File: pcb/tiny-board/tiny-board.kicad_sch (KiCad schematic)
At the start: 22 parts, among them J1 USB_B, J2 EXPBUS1, J4 Atmel-JTAG-10, SW1 RESET, SW2 NMI, SW3 SW_SPDT, U1 74AC14, U2 W65C02, U3 ATF1502AS-PLCC44, X1 14 MHz

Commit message: Saving tiny board design
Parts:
- removed J4: Atmel-JTAG-10, Connector_IDC:IDC-Header_2x05_P2.54mm_Vertical, symbol atf1504_plcc44_breakout:Atmel-JTAG-10
- removed U3: ATF1502AS-PLCC44, Package_LCC:PLCC-44_THT-Socket, symbol atf1504as-plcc44:ATF1504AS-xJx44
- added C2: 100nF, Capacitor_THT:C_Disc_D5.0mm_W2.5mm_P5.00mm, symbol Device:C
- added U3: CD74HC688, Package_DIP:DIP-20_W7.62mm_Socket, symbol 74xx:74HC688
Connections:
- net A10: now also U3.6 (P2)
- net A11: now also U3.8 (P3)
- net A12: now also U3.11 (P4)
- net A13: now also U3.13 (P5)
- net A14: now also U3.15 (P6)
- net A15: now also U3.17 (P7)
- net A8: now also U3.2 (P0)
- net A9: now also U3.4 (P1)
- net GND: now also C2.2, U3.1 (G), U3.10 (GND), U3.18 (R7)
- net VCC: now also C2.1, U3.12 (R4), U3.14 (R5), U3.16 (R6), U3.20 (VCC), U3.3 (R0), U3.5 (R1), U3.7 (R2), U3.9 (R3)
- net ~{I/O}: now also U3.19 (P=R)
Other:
- note added: "0x7F"
- note added: "0x7FXX"
- note added: "Single 74HC688 is used to map 0x7F00 - 0x7FF as the I/O space."

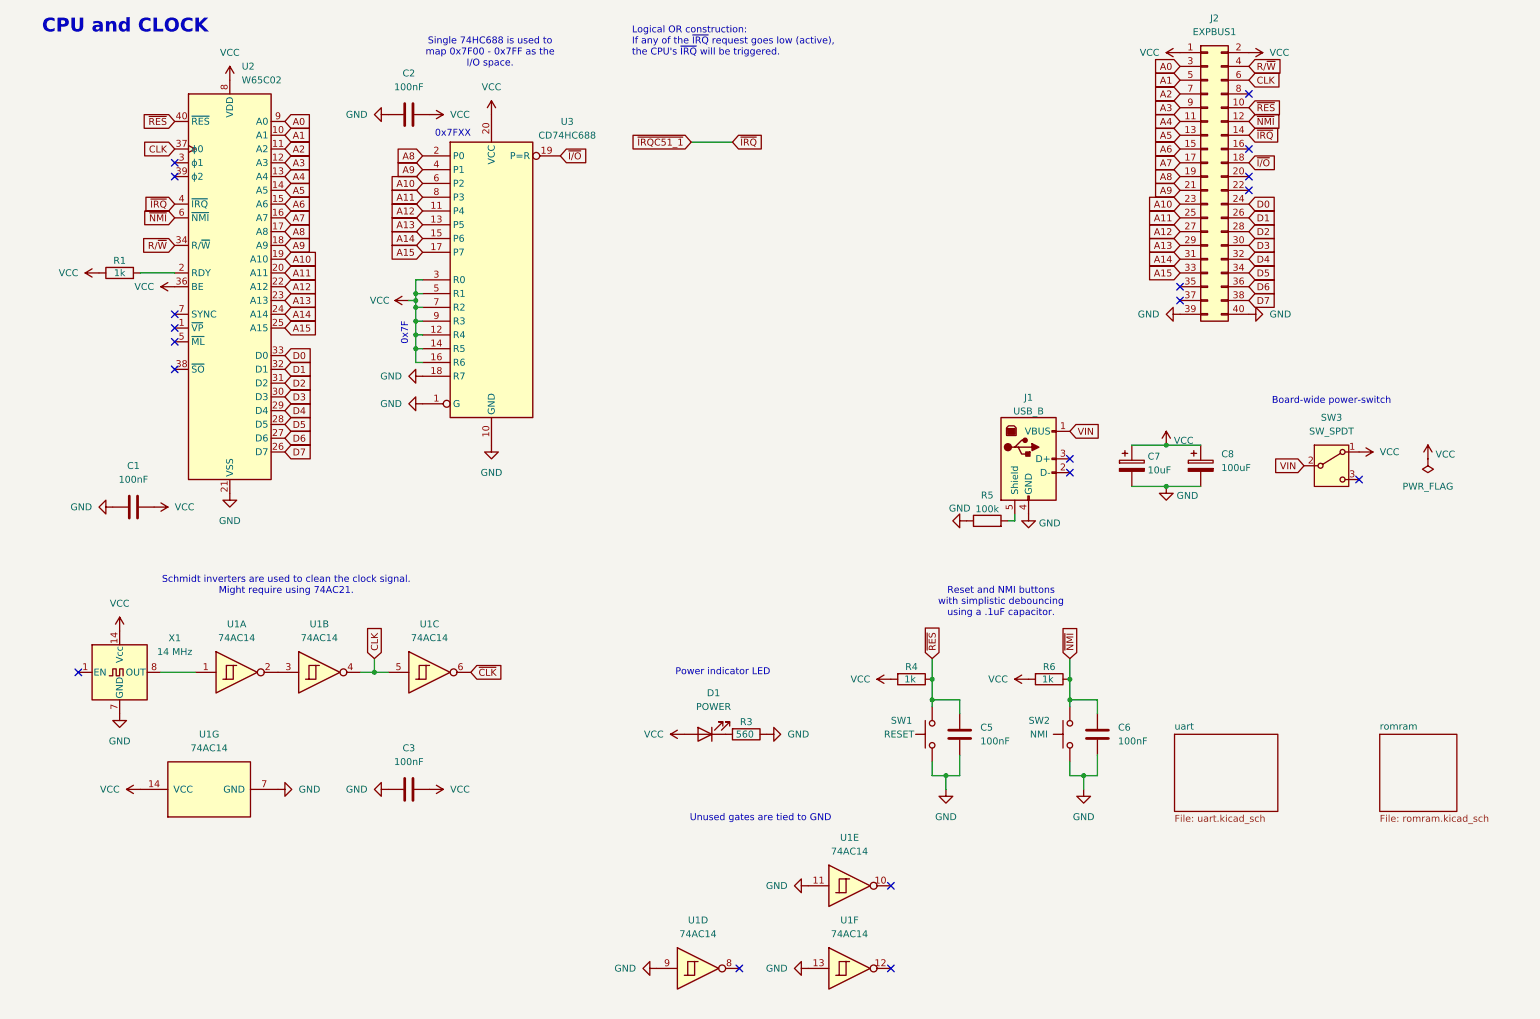
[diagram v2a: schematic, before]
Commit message: Revising TINY board and writing CUPL
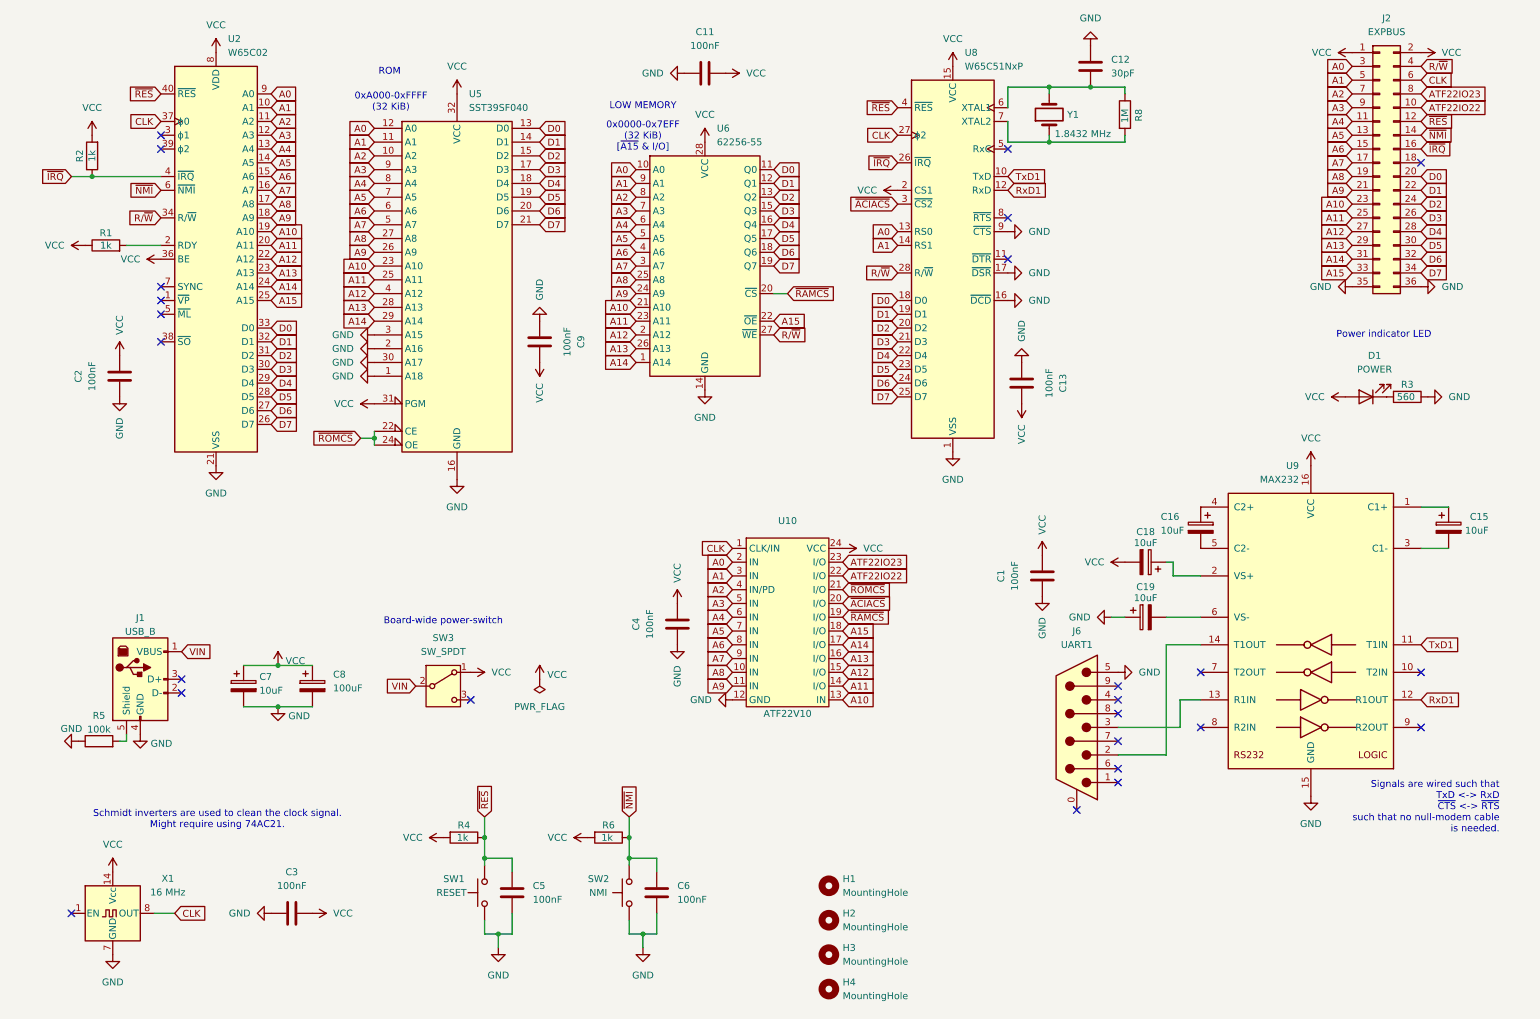
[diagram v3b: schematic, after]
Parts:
- removed J2: EXPBUS1, Connector_PinHeader_2.54mm:PinHeader_2x20_P2.54mm_Vertical, symbol Connector_Generic:Conn_02x20_Odd_Even
- removed U1: 74AC14, Package_DIP:DIP-14_W7.62mm_Socket, symbol 74xx:74HC14
- removed U3: CD74HC688, Package_DIP:DIP-20_W7.62mm_Socket, symbol 74xx:74HC688
- added C11, C13, C4, C9: 100nF, Capacitor_THT:C_Disc_D5.0mm_W2.5mm_P5.00mm, symbol Device:C
- added C12: 30pF, Capacitor_THT:C_Disc_D5.0mm_W2.5mm_P5.00mm, symbol Device:C
- added C15, C16, C18, C19: 10uF, Capacitor_THT:CP_Radial_D5.0mm_P2.50mm, symbol Device:C_Polarized
- added H1, H2, H3, H4: MountingHole, MountingHole:MountingHole_3.2mm_M3_DIN965_Pad_TopOnly, symbol Mechanical:MountingHole
- added J2: EXPBUS, Connector_PinHeader_2.54mm:PinHeader_2x18_P2.54mm_Vertical, symbol Connector_Generic:Conn_02x18_Odd_Even
- added J6: UART1, Connector_Dsub:DSUB-9_Pins_Horizontal_P2.77x2.84mm_EdgePinOffset4.94mm_Housed_MountingHolesOffset4.94mm, symbol Connector:DE9_Pins_MountingHoles
- added R2: 1k, Resistor_THT:R_Axial_DIN0207_L6.3mm_D2.5mm_P7.62mm_Horizontal, symbol Device:R
- added R8: 1M, Resistor_THT:R_Axial_DIN0207_L6.3mm_D2.5mm_P7.62mm_Horizontal, symbol Device:R
- added U10: ATF22V10, Package_DIP:DIP-24_W7.62mm_Socket, symbol atf22v10:ATF22V10
- added U5: SST39SF040, Package_DIP:DIP-32_W15.24mm_Socket, symbol Memory_Flash:SST39SF040
- added U6: 62256-55, Package_DIP:DIP-28_W15.24mm_Socket, symbol Memory_RAM:CY62256-70PC
- added U8: W65C51NxP, Package_DIP:DIP-28_W15.24mm_Socket, symbol 65xx-library:W65C51NxP
- added U9: MAX232, Package_DIP:DIP-16_W7.62mm_Socket, symbol Interface_UART:MAX232
- added Y1: 1.8432 MHz, Crystal:Crystal_HC50_Vertical, symbol Device:Crystal
- C7: footprint Capacitor_THT:CP_Radial_D6.3mm_P2.50mm -> Capacitor_THT:CP_Radial_D5.0mm_P2.50mm
- X1: value 14 MHz -> 16 MHz
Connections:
- net A0: now also J2.3 (Pin_3), U10.2 (IN), U5.12 (A0), U6.10 (A0), U8.13 (RS0)
- net A1: now also J2.5 (Pin_5), U10.3 (IN), U5.11 (A1), U6.9 (A1), U8.14 (RS1)
- net A10: now also J2.23 (Pin_23), U10.13 (IN), U5.23 (A10), U6.21 (A10)
- net A11: now also J2.25 (Pin_25), U10.14 (I/O), U5.25 (A11), U6.23 (A11)
- net A12: now also J2.27 (Pin_27), U10.15 (I/O), U5.4 (A12), U6.2 (A12)
- net A13: now also J2.29 (Pin_29), U10.16 (I/O), U5.28 (A13), U6.26 (A13)
- net A14: now also J2.31 (Pin_31), U10.17 (I/O), U5.29 (A14), U6.1 (A14)
- net A15: now also J2.33 (Pin_33), U10.18 (I/O), U6.22 (~{OE})
- net A2: now also J2.7 (Pin_7), U10.4 (IN/PD), U5.10 (A2), U6.8 (A2)
- net A3: now also J2.9 (Pin_9), U10.5 (IN), U5.9 (A3), U6.7 (A3)
- net A4: now also J2.11 (Pin_11), U10.6 (IN), U5.8 (A4), U6.6 (A4)
- net A5: now also J2.13 (Pin_13), U10.7 (IN), U5.7 (A5), U6.5 (A5)
- net A6: now also J2.15 (Pin_15), U10.8 (IN), U5.6 (A6), U6.4 (A6)
- net A7: now also J2.17 (Pin_17), U10.9 (IN), U5.5 (A7), U6.3 (A7)
- net A8: now also J2.19 (Pin_19), U10.10 (IN), U5.27 (A8), U6.25 (A8)
- net A9: now also J2.21 (Pin_21), U10.11 (IN), U5.26 (A9), U6.24 (A9)
- net CLK: now also X1.8 (OUT), J2.6 (Pin_6), U10.1 (CLK/IN), U8.27 (ϕ2)
- net D0: now also J2.20 (Pin_20), U5.13 (D0), U6.11 (Q0), U8.18 (D0)
- net D1: now also J2.22 (Pin_22), U5.14 (D1), U6.12 (Q1), U8.19 (D1)
- net D2: now also J2.24 (Pin_24), U5.15 (D2), U6.13 (Q2), U8.20 (D2)
- net D3: now also J2.26 (Pin_26), U5.17 (D3), U6.15 (Q3), U8.21 (D3)
- net D4: now also J2.28 (Pin_28), U5.18 (D4), U6.16 (Q4), U8.22 (D4)
- net D5: now also J2.30 (Pin_30), U5.19 (D5), U6.17 (Q5), U8.23 (D5)
- net D6: now also J2.32 (Pin_32), U5.20 (D6), U6.18 (Q6), U8.24 (D6)
- net D7: now also J2.34 (Pin_34), U5.21 (D7), U6.19 (Q7), U8.25 (D7)
- net GND: now also C11.2, C12.1, C13.2, C19.1, C4.2, C9.2, J2.35 (Pin_35), J2.36 (Pin_36), J6.5, U10.12 (GND), U5.1 (A18), U5.16 (GND), U5.2 (A16), U5.3 (A15), U5.30 (A17), U6.14 (GND), U8.1 (VSS), U8.16 (~{DCD}), U8.17 (~{DSR}), U8.9 (~{CTS}), U9.15 (GND)
- net R/~{W}: now also J2.4 (Pin_4), U6.27 (~{WE}), U8.28 (R/~{W})
- net VCC: now also C11.1, C13.1, C18.2, C4.1, C9.1, J2.1 (Pin_1), J2.2 (Pin_2), R2.2, U10.24 (VCC), U5.31 (PGM), U5.32 (VCC), U6.28 (VCC), U8.15 (VCC), U8.2 (CS1), U9.16 (VCC)
- net ~{NMI}: now also J2.14 (Pin_14)
- net ~{RES}: now also J2.12 (Pin_12), U8.4 (~{RES})
- net ~{IRQC51_1} renamed ~{IRQ}
- net ~{IRQ}: now also J2.16 (Pin_16), R2.1, U8.26 (~{IRQ})
- new net: R8.2, U8.7 (XTAL2), Y1.1
- new net: C12.2, R8.1, U8.6 (XTAL1), Y1.2
- new net: C15.1, U9.1 (C1+)
- new net: J6.3, U9.13 (R1IN)
- new net: J6.2, U9.14 (T1OUT)
- new net: C18.1, U9.2 (VS+)
- new net: C15.2, U9.3 (C1-)
- new net: C16.1, U9.4 (C2+)
- new net: C16.2, U9.5 (C2-)
- new net: C19.2, U9.6 (VS-)
- new net ATF22IO22: J2.10 (Pin_10), U10.22 (I/O)
- new net ATF22IO23: J2.8 (Pin_8), U10.23 (I/O)
- new net RxD1: U8.12 (RxD), U9.12 (R1OUT)
- new net TxD1: U8.10 (TxD), U9.11 (T1IN)
- new net ~{ACIACS}: U10.20 (I/O), U8.3 (~{CS2})
- new net ~{RAMCS}: U10.19 (I/O), U6.20 (~{CS})
- new net ~{ROMCS}: U10.21 (I/O), U5.22 (CE), U5.24 (OE)
- no-connect marks 19 -> 25
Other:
- removed sheet romram
- removed sheet uart
- note added: "0x0000-0x7EFF (32 KiB) [~{A15} & I/O]"
- note added: "0xA000-0xFFFF (32 KiB)"
- note added: "LOW MEMORY"
- note added: "ROM"
- note added: "Signals are wired such that TxD <-> RxD ~{CTS} <-> ~{RTS} such that no null-modem cable is needed."
- note removed: "0x7F"
- note removed: "0x7FXX"
- note removed: "CPU and CLOCK"
- note removed: "Logical OR construction: If any of the ~{IRQ} request goes low (active), the CPU's ~{IRQ} will be triggered."
- note removed: "Reset and NMI buttons with simplistic debouncing using a .1uF capacitor."
- note removed: "Single 74HC688 is used to map 0x7F00 - 0x7FF as the I/O space."
- note removed: "Unused gates are tied to GND"
- title: ByteCradle 6502 - CPU & CLOCK -> ByteCradle 6502 - TINY
- moved on the sheet: C1, C3, C5, C6, C7, C8, D1, J1, R1, R3, R4, R5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

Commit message: Integrating monitor
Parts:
- U5: symbol Memory_Flash:SST39SF040 -> Memory_Flash:SST39SF010
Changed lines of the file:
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@@
 	)
 	(symbol
-		(lib_id "Memory_Flash:SST39SF040")
+		(lib_id "Memory_Flash:SST39SF010")
 		(at 90.17 66.04 0)
 		(unit 1)
@@
 		(fields_autoplaced yes)
 		(property "Reference" "U5"
-			(at 92.3641 29.21 0)
+			(at 92.3133 29.21 0)
 			(effects
 				(font
@@
 		)
 		(property "Value" "SST39SF040"
-			(at 92.3641 31.75 0)
+			(at 92.3133 31.75 0)
 			(effects
 				(font
@@
 			)
 		)
-		(property "Description" "Silicon Storage Technology (SSF) 512k x 8 Flash ROM"
+		(property "Description" "Silicon Storage Technology (SSF) 128k x 8 Flash ROM"
 			(at 90.17 66.04 0)
 			(effects

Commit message: Integrating CIA CPLD for tiny board
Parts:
- U5: value SST39SF040 -> SST39SF010
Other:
- note added: "0x8000-0xFFFF (32 KiB)"
- note removed: "0xA000-0xFFFF (32 KiB)"
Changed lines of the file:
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@@
 		)
 	)
-	(text "0xA000-0xFFFF\n(32 KiB)"
+	(text "0x8000-0xFFFF\n(32 KiB)"
 		(exclude_from_sim no)
 		(at 77.978 30.734 0)
@@
 			)
 		)
-		(property "Value" "SST39SF040"
+		(property "Value" "SST39SF010"
 			(at 92.3133 31.75 0)
 			(effects

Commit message: Revising board and integrating DS1813
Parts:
- removed C5: 100nF, Capacitor_THT:C_Disc_D5.0mm_W2.5mm_P5.00mm, symbol Device:C
- removed R4: 1k, Resistor_THT:R_Axial_DIN0207_L6.3mm_D2.5mm_P7.62mm_Horizontal, symbol Device:R
- added U11: DS1813, Package_TO_SOT_THT:TO-92, symbol Connector:Conn_01x03_Pin
- C8: value 100uF -> 220uF
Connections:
- net GND: now also U11.3 (Pin_3)
- net VCC: now also U11.2 (Pin_2)
- net ~{RES}: now also U11.1 (Pin_1)
- net ATF22IO22 renamed B1
- net ATF22IO23 renamed B2
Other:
- moved on the sheet: SW1

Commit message: Expanding README.md
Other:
- moved on the sheet: C1, C15, C16, C18, C19, D1, J6, R3, U9

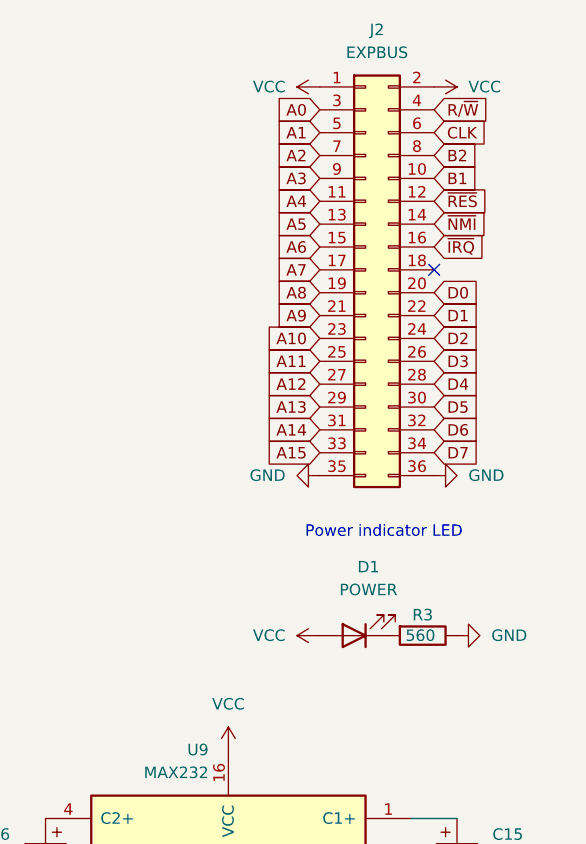
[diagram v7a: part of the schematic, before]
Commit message: Revising tinyboard (REV2) and adding daughterboard with LEDs
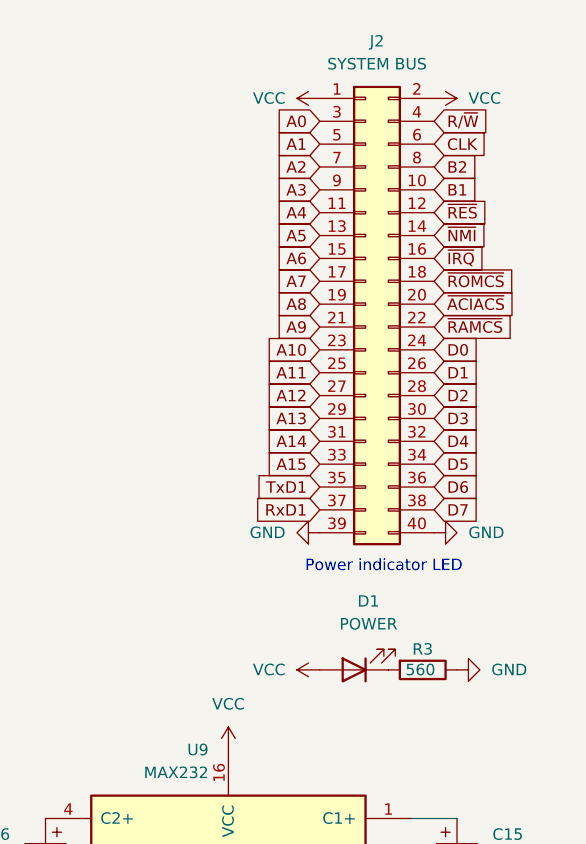
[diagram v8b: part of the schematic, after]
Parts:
- J2: value EXPBUS -> SYSTEM BUS; footprint Connector_PinHeader_2.54mm:PinHeader_2x18_P2.54mm_Vertical -> Connector_PinHeader_2.54mm:PinHeader_2x20_P2.54mm_Vertical; symbol Connector_Generic:Conn_02x18_Odd_Even -> Connector_Generic:Conn_02x20_Odd_Even
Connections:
- net D0: now also J2.24 (Pin_24); no longer J2.20 (Pin_20)
- net D1: now also J2.26 (Pin_26); no longer J2.22 (Pin_22)
- net D2: now also J2.28 (Pin_28); no longer J2.24 (Pin_24)
- net D3: now also J2.30 (Pin_30); no longer J2.26 (Pin_26)
- net D4: now also J2.32 (Pin_32); no longer J2.28 (Pin_28)
- net D5: now also J2.34 (Pin_34); no longer J2.30 (Pin_30)
- net D6: now also J2.36 (Pin_36); no longer J2.32 (Pin_32)
- net D7: now also J2.38 (Pin_38); no longer J2.34 (Pin_34)
- net GND: now also J2.39 (Pin_39), J2.40 (Pin_40); no longer J2.35 (Pin_35), J2.36 (Pin_36)
- net RxD1: now also J2.37 (Pin_37)
- net TxD1: now also J2.35 (Pin_35)
- net ~{ACIACS}: now also J2.20 (Pin_20)
- net ~{RAMCS}: now also J2.22 (Pin_22)
- net ~{ROMCS}: now also J2.18 (Pin_18)
- no-connect marks 25 -> 24
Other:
- moved on the sheet: D1, R3
